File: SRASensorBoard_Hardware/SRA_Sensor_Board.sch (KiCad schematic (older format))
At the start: 70 parts, among them J1 USB_B_Micro, Q1 CSD17305Q5A, U1 LM3478MMX_NOPB, U2 OKI, U3 OKI, U4 TM4C129E_Launchpad, U5 MAX232, U6 IRF7821PbF

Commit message: Cleaned Some Things
Signatures and shem visual changes
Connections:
- wire segments 186 -> 185
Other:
- moved on the sheet: C1, C10, C11, C2, C3, C8, C9, D1, D10, D11, D12, D13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

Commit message: Updates
Updated traces on board

Changed resistor values to be in compliance with best practices

Regenerated STEP and GERBER files for updated board

Added TIVA and Connections text files
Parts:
- R10, R11, R12, R13, R14, R15, R16, R17, R18, R19, R20, R23, R24, R7: value 500 -> 510
- R9: value 500 -> 330
- U4: symbol MRDT_Shields:TM4C129E_Launchpad -> SRA_Sensor_Board-rescue:TM4C129E_Launchpad-MRDT_Shields
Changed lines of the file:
@@
 P 14850 5200
 F 0 "R20" H 14920 5246 50  0000 L CNN
-F 1 "500" H 14920 5155 50  0000 L CNN
+F 1 "510" H 14920 5155 50  0000 L CNN
 F 2 "Resistor_SMD:R_0603_1608Metric_Pad1.05x0.95mm_HandSolder" V 14780 5200 50  0001 C CNN
 F 3 "~" H 14850 5200 50  0001 C CNN
@@
 P 14500 5200
 F 0 "R19" H 14570 5246 50  0000 L CNN
-F 1 "500" H 14570 5155 50  0000 L CNN
+F 1 "510" H 14570 5155 50  0000 L CNN
 F 2 "Resistor_SMD:R_0603_1608Metric_Pad1.05x0.95mm_HandSolder" V 14430 5200 50  0001 C CNN
 F 3 "~" H 14500 5200 50  0001 C CNN
@@
 P 14150 5200
 F 0 "R18" H 14220 5246 50  0000 L CNN
-F 1 "500" H 14220 5155 50  0000 L CNN
+F 1 "510" H 14220 5155 50  0000 L CNN
 F 2 "Resistor_SMD:R_0603_1608Metric_Pad1.05x0.95mm_HandSolder" V 14080 5200 50  0001 C CNN
 F 3 "~" H 14150 5200 50  0001 C CNN
@@
 P 13800 5200
 F 0 "R17" H 13870 5246 50  0000 L CNN
-F 1 "500" H 13870 5155 50  0000 L CNN
+F 1 "510" H 13870 5155 50  0000 L CNN
 F 2 "Resistor_SMD:R_0603_1608Metric_Pad1.05x0.95mm_HandSolder" V 13730 5200 50  0001 C CNN
 F 3 "~" H 13800 5200 50  0001 C CNN
@@
 P 13450 5200
 F 0 "R16" H 13520 5246 50  0000 L CNN
-F 1 "500" H 13520 5155 50  0000 L CNN
+F 1 "510" H 13520 5155 50  0000 L CNN
 F 2 "Resistor_SMD:R_0603_1608Metric_Pad1.05x0.95mm_HandSolder" V 13380 5200 50  0001 C CNN
 F 3 "~" H 13450 5200 50  0001 C CNN
@@
 P 13100 5200
 F 0 "R15" H 13170 5246 50  0000 L CNN
-F 1 "500" H 13170 5155 50  0000 L CNN
+F 1 "510" H 13170 5155 50  0000 L CNN
 F 2 "Resistor_SMD:R_0603_1608Metric_Pad1.05x0.95mm_HandSolder" V 13030 5200 50  0001 C CNN
 F 3 "~" H 13100 5200 50  0001 C CNN
@@
 P 11100 5200
 F 0 "R13" H 11170 5246 50  0000 L CNN
-F 1 "500" H 11170 5155 50  0000 L CNN
+F 1 "510" H 11170 5155 50  0000 L CNN
 F 2 "Resistor_SMD:R_0603_1608Metric_Pad1.05x0.95mm_HandSolder" V 11030 5200 50  0001 C CNN
 F 3 "~" H 11100 5200 50  0001 C CNN
@@
 P 10750 5200
 F 0 "R12" H 10820 5246 50  0000 L CNN
-F 1 "500" H 10820 5155 50  0000 L CNN
+F 1 "510" H 10820 5155 50  0000 L CNN
 F 2 "Resistor_SMD:R_0603_1608Metric_Pad1.05x0.95mm_HandSolder" V 10680 5200 50  0001 C CNN
 F 3 "~" H 10750 5200 50  0001 C CNN
@@
 P 10400 5200
 F 0 "R11" H 10470 5246 50  0000 L CNN
-F 1 "500" H 10470 5155 50  0000 L CNN
+F 1 "510" H 10470 5155 50  0000 L CNN
 F 2 "Resistor_SMD:R_0603_1608Metric_Pad1.05x0.95mm_HandSolder" V 10330 5200 50  0001 C CNN
 F 3 "~" H 10400 5200 50  0001 C CNN
@@
 P 12700 5200
 F 0 "R14" H 12770 5246 50  0000 L CNN
-F 1 "500" H 12770 5155 50  0000 L CNN
+F 1 "510" H 12770 5155 50  0000 L CNN
 F 2 "Resistor_SMD:R_0603_1608Metric_Pad1.05x0.95mm_HandSolder" V 12630 5200 50  0001 C CNN
 F 3 "~" H 12700 5200 50  0001 C CNN
@@
 P 10050 5200
 F 0 "R10" H 10120 5246 50  0000 L CNN
-F 1 "500" H 10120 5155 50  0000 L CNN
+F 1 "510" H 10120 5155 50  0000 L CNN
 F 2 "Resistor_SMD:R_0603_1608Metric_Pad1.05x0.95mm_HandSolder" V 9980 5200 50  0001 C CNN
 F 3 "~" H 10050 5200 50  0001 C CNN
@@
 P 9700 5200
 F 0 "R9" H 9770 5246 50  0000 L CNN
-F 1 "500" H 9770 5155 50  0000 L CNN
+F 1 "330" H 9770 5155 50  0000 L CNN
 F 2 "Resistor_SMD:R_0603_1608Metric_Pad1.05x0.95mm_HandSolder" V 9630 5200 50  0001 C CNN
 F 3 "~" H 9700 5200 50  0001 C CNN
@@
 P 12300 5200
 F 0 "R24" H 12370 5246 50  0000 L CNN
-F 1 "500" H 12370 5155 50  0000 L CNN
+F 1 "510" H 12370 5155 50  0000 L CNN
 F 2 "Resistor_SMD:R_0603_1608Metric_Pad1.05x0.95mm_HandSolder" V 12230 5200 50  0001 C CNN
 F 3 "~" H 12300 5200 50  0001 C CNN
@@
 P 11900 5200
 F 0 "R23" H 11970 5246 50  0000 L CNN
-F 1 "500" H 11970 5155 50  0000 L CNN
+F 1 "510" H 11970 5155 50  0000 L CNN
 F 2 "Resistor_SMD:R_0603_1608Metric_Pad1.05x0.95mm_HandSolder" V 11830 5200 50  0001 C CNN
 F 3 "~" H 11900 5200 50  0001 C CNN
@@
 P 11500 5200
 F 0 "R7" H 11570 5246 50  0000 L CNN
-F 1 "500" H 11570 5155 50  0000 L CNN
+F 1 "510" H 11570 5155 50  0000 L CNN
 F 2 "Resistor_SMD:R_0603_1608Metric_Pad1.05x0.95mm_HandSolder" V 11430 5200 50  0001 C CNN
 F 3 "~" H 11500 5200 50  0001 C CNN
@@
 	9150 2650 9250 2650
 $Comp
-L MRDT_Shields:TM4C129E_Launchpad U4
+L SRA_Sensor_Board-rescue:TM4C129E_Launchpad-MRDT_Shields U4
 U 5 1 5DD6BB3C
 P 9450 3600
@@
 $EndComp
 $Comp
-L MRDT_Shields:TM4C129E_Launchpad U4
+L SRA_Sensor_Board-rescue:TM4C129E_Launchpad-MRDT_Shields U4
 U 6 1 5DD2931F
 P 9950 3600

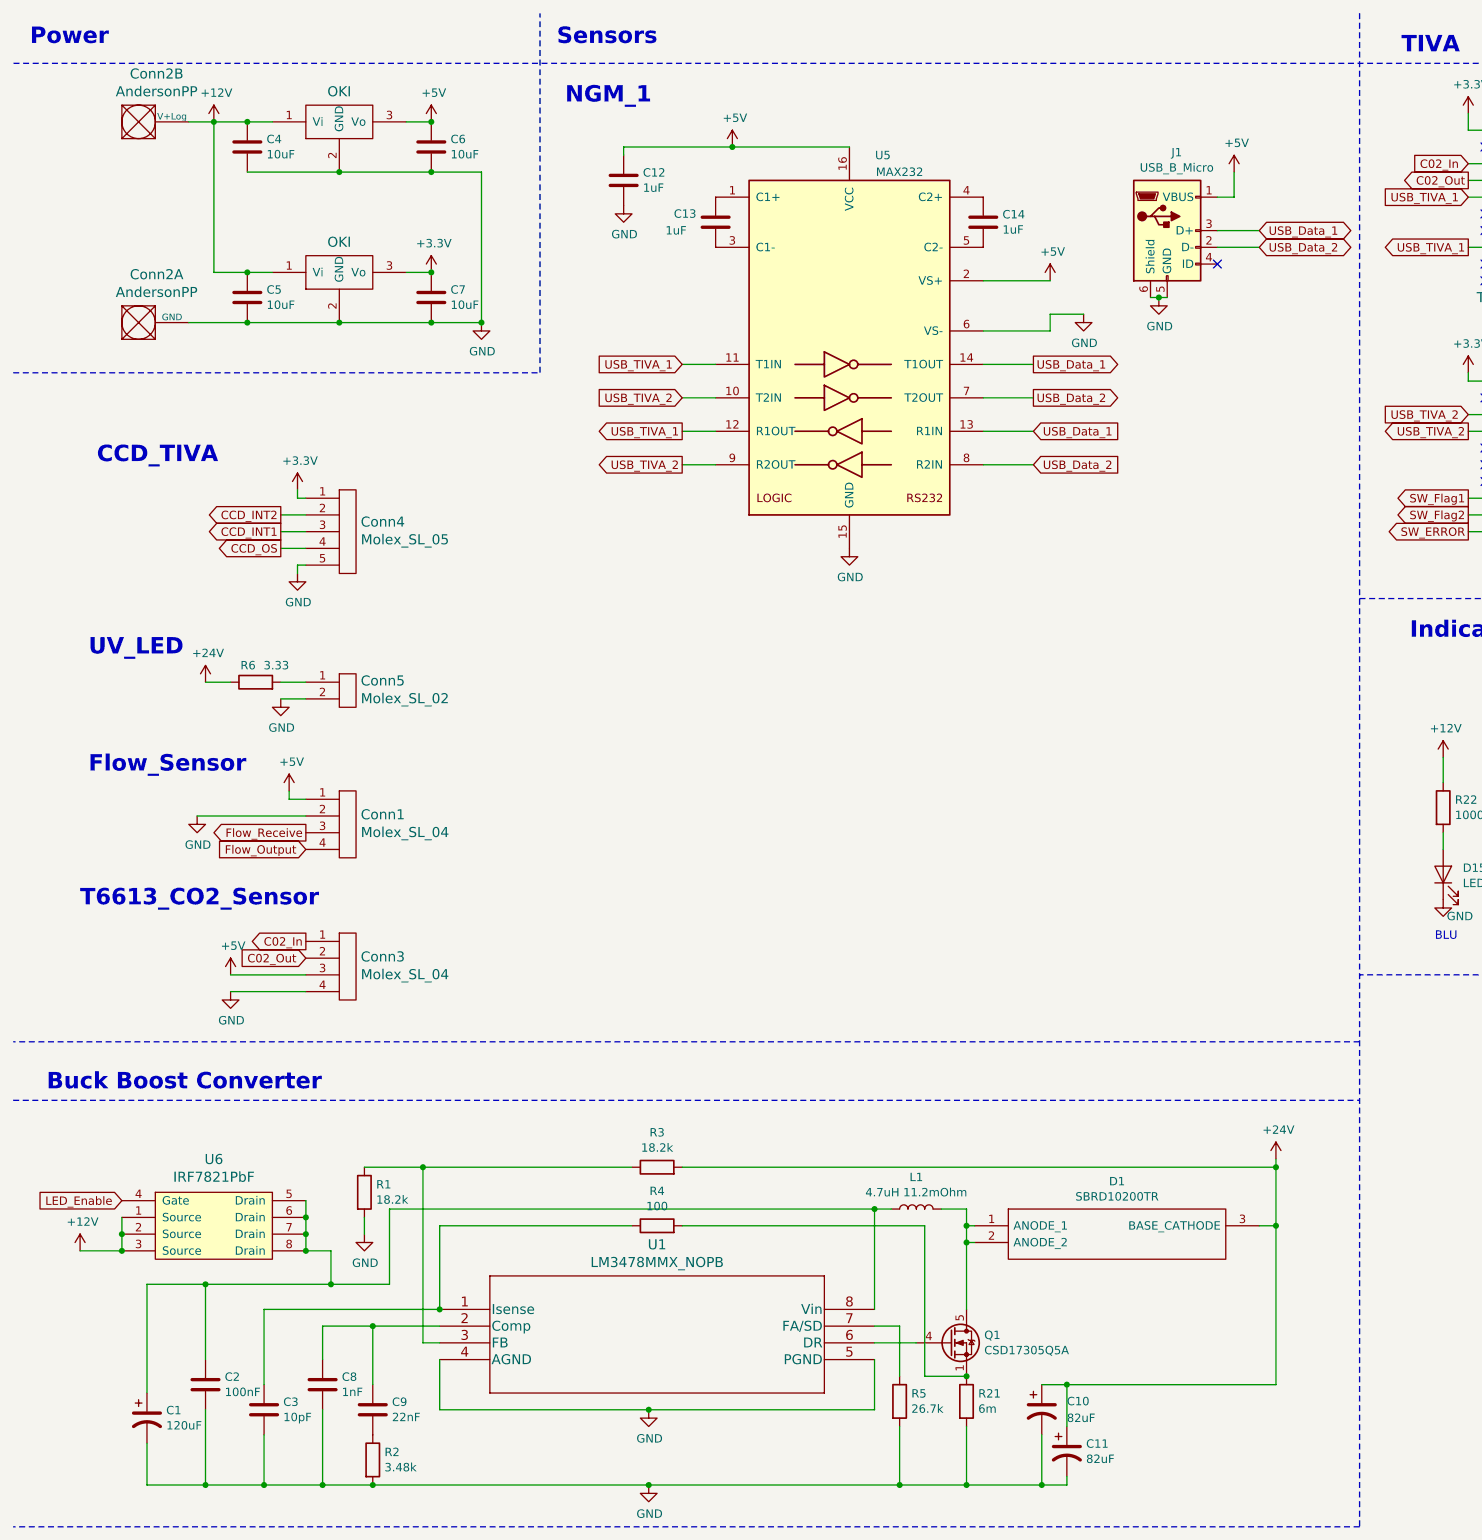
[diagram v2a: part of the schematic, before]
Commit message: Some Rev 2 schematic changes. Tivas and indicator leds still need updating
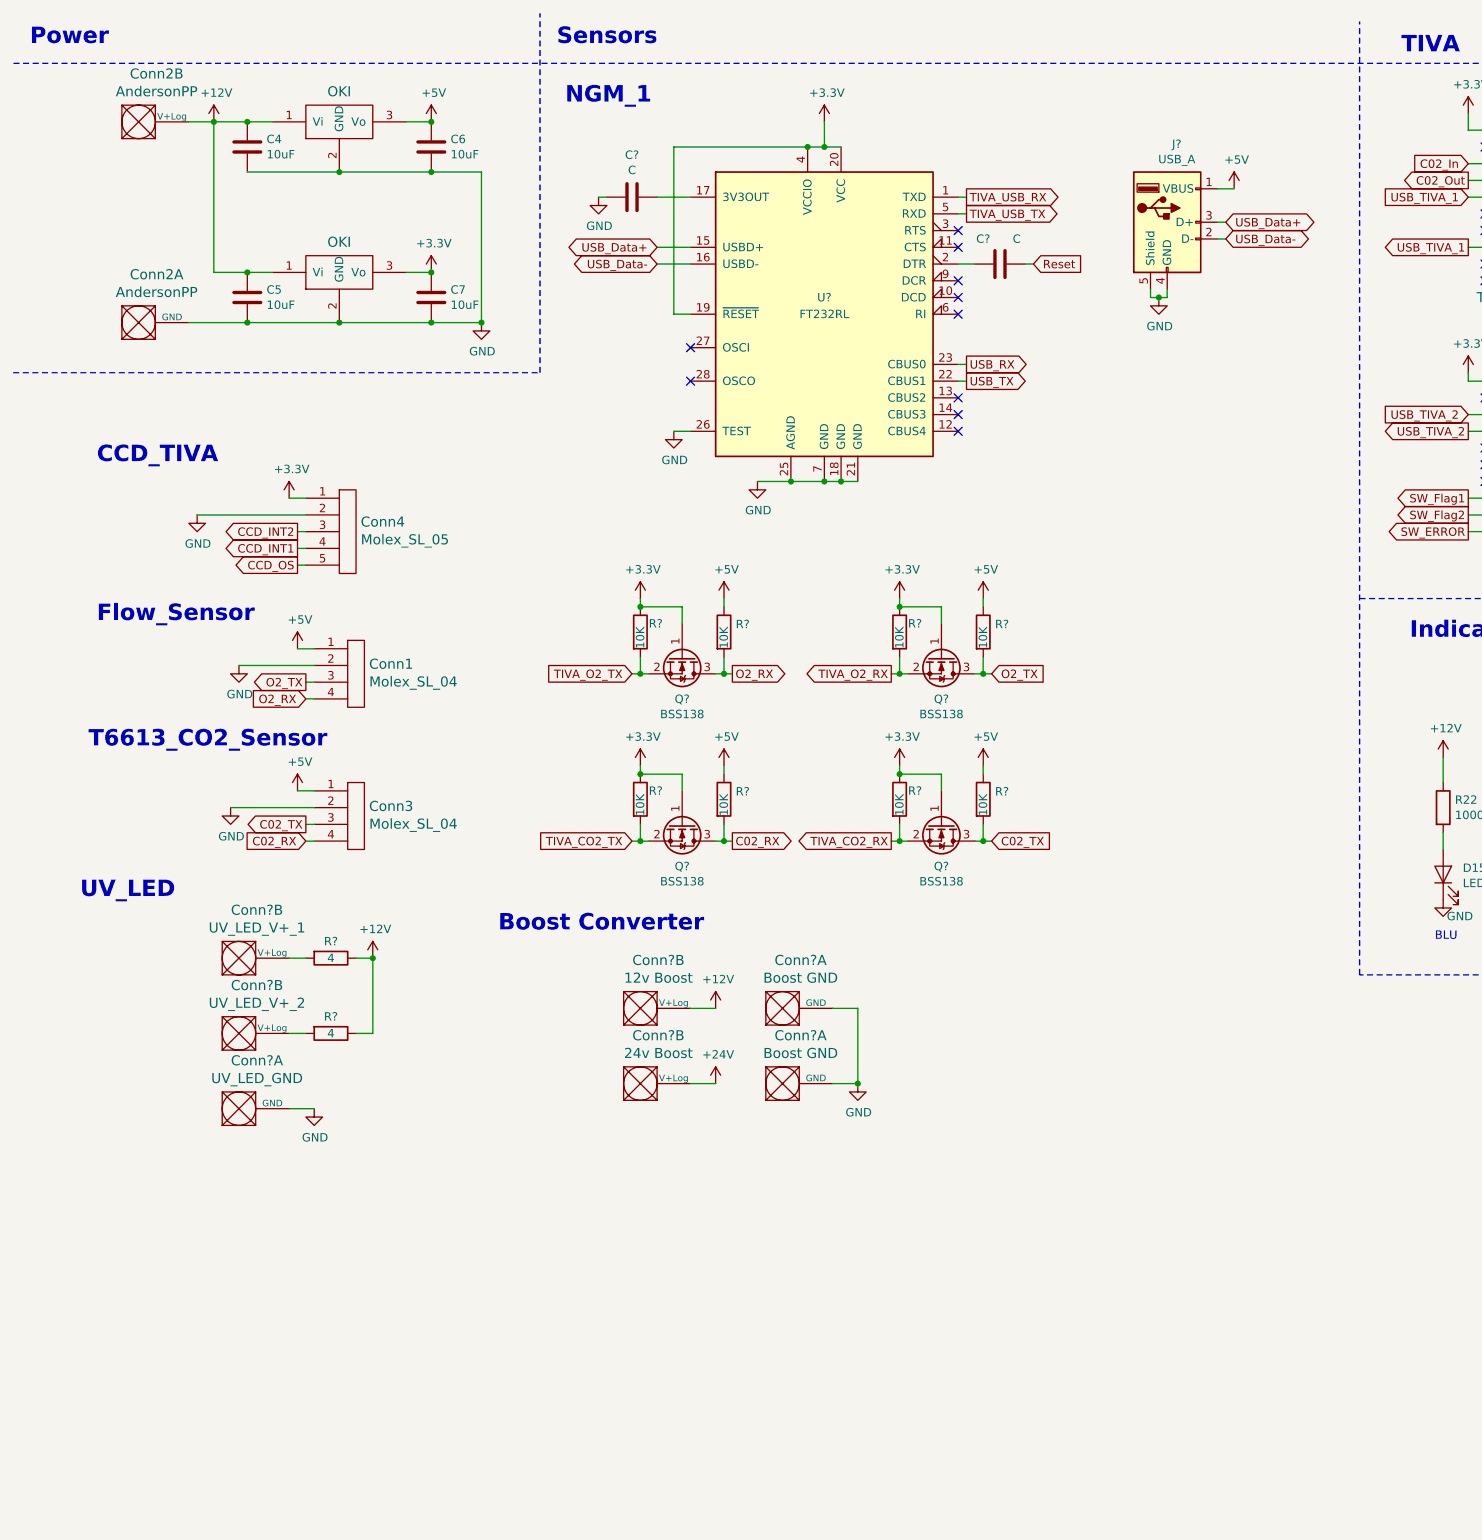
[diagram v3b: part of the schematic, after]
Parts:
- removed C1: 120uF, Capacitor_SMD:C_0603_1608Metric_Pad1.05x0.95mm_HandSolder, symbol Device:CP1
- removed C10, C11: 82uF, Capacitor_SMD:C_0603_1608Metric_Pad1.05x0.95mm_HandSolder, symbol Device:CP1
- removed C12, C13, C14: 1uF, Capacitor_SMD:C_0603_1608Metric_Pad1.05x0.95mm_HandSolder, symbol Device:C
- removed C2: 100nF, Capacitor_SMD:C_0603_1608Metric_Pad1.05x0.95mm_HandSolder, symbol Device:C
- removed C3: 10pF, Capacitor_SMD:C_0603_1608Metric_Pad1.05x0.95mm_HandSolder, symbol Device:C
- removed C8: 1nF, Capacitor_SMD:C_0603_1608Metric_Pad1.05x0.95mm_HandSolder, symbol Device:C
- removed C9: 22nF, Capacitor_SMD:C_0603_1608Metric_Pad1.05x0.95mm_HandSolder, symbol Device:C
- removed Conn5: Molex_SL_02, MRDT_Connectors:MOLEX_SL_02_Vertical, symbol MRDT_Connectors:Molex_SL_02
- removed D1: SBRD10200TR, MRDT_ICs:SMC_DPAK, symbol SBRD10200TR:SBRD10200TR
- removed J1: USB_B_Micro, Connector_USB:USB_Micro-B_Molex-105017-0001, symbol Connector:USB_B_Micro
- removed L1: 4.7uH 11.2mOhm, custom:Donald_Shaw_SRP1270, symbol Device:L
- removed Q1: CSD17305Q5A, Package_TO_SOT_SMD:TDSON-8-1, symbol Transistor_FET:CSD17305Q5A
- removed R1, R3: 18.2k, Resistor_SMD:R_0603_1608Metric_Pad1.05x0.95mm_HandSolder, symbol Device:R
- removed R2: 3.48k, Resistor_SMD:R_0603_1608Metric_Pad1.05x0.95mm_HandSolder, symbol Device:R
- removed R21: 6m, Resistor_SMD:R_0603_1608Metric_Pad1.05x0.95mm_HandSolder, symbol Device:R
- removed R4: 100, Resistor_SMD:R_0603_1608Metric_Pad1.05x0.95mm_HandSolder, symbol Device:R
- removed R5: 26.7k, Resistor_SMD:R_0603_1608Metric_Pad1.05x0.95mm_HandSolder, symbol Device:R
- removed R6: 3.33, Resistor_SMD:R_0603_1608Metric_Pad1.05x0.95mm_HandSolder, symbol Device:R
- removed U1: LM3478MMX_NOPB, custom:LM3478MMX&slash_NOPB, symbol SRA_Sensor_Board-rescue:LM3478MMX_NOPB-2019-10-10_22-50-45
- removed U5: MAX232, footprints:MAX232DR, symbol Interface_UART:MAX232
- removed U6: IRF7821PbF, footprints:IRF7821PBF, symbol MRDT_ICs:IRF7821PbF
- added C? (x2): C, symbol Device:C
- added Conn?: UV_LED_GND, symbol MRDT_Connectors:AndersonPP
- added Conn?: UV_LED_V+_1, symbol MRDT_Connectors:AndersonPP
- added Conn?: UV_LED_V+_2, symbol MRDT_Connectors:AndersonPP
- added Conn?: 12v Boost, symbol MRDT_Connectors:AndersonPP
- added Conn?: 24v Boost, symbol MRDT_Connectors:AndersonPP
- added Conn? (x2): Boost GND, symbol MRDT_Connectors:AndersonPP
- added J?: USB_A, symbol Connector:USB_A
- added Q? (x4): BSS138, Package_TO_SOT_SMD:SOT-23, symbol Transistor_FET:BSS138
- added R? (x8): 10K, symbol Device:R
- added R? (x2): 4, symbol Device:R
- added U?: FT232RL, Package_SO:SSOP-28_5.3x10.2mm_P0.65mm, symbol Interface_USB:FT232RL
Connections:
- net +12V: now also Conn?.2 (V+Log), R?.1, R?.1
- net +24V: now also Conn?.2 (V+Log)
- net +3V3: now also Q?.1 (G), Q?.1 (G), Q?.1 (G), Q?.1 (G), R?.1, R?.1, R?.1, R?.1, U?.19 (~RESET~), U?.20 (VCC), U?.4 (VCCIO)
- net +5V: now also Conn3.1, J?.1 (VBUS), R?.1, R?.1, R?.1, R?.1; no longer Conn3.3
- net C02_In: no longer Conn3.1
- net C02_Out: no longer Conn3.2
- net CCD_INT1: now also Conn4.4; no longer Conn4.3
- net CCD_INT2: now also Conn4.3; no longer Conn4.2
- net CCD_OS: now also Conn4.5; no longer Conn4.4
- net Flow_Output: no longer Conn1.4
- net Flow_Receive: no longer Conn1.3
- net GND: now also Conn3.2, Conn4.2, C?.2, Conn?.1 (GND), Conn?.1 (GND), Conn?.1 (GND), J?.4 (GND), J?.5 (Shield), U?.18 (GND), U?.21 (GND), U?.25 (AGND), U?.26 (TEST), U?.7 (GND); no longer Conn3.4, Conn4.5
- new net: C?.1, U?.17 (3V3OUT)
- new net: C?.2, U?.2 (DTR)
- new net: Conn?.2 (V+Log), R?.2 (x2)
- new net C02_RX: Conn3.4, Q?.3 (D), R?.2
- new net C02_TX: Conn3.3, Q?.3 (D), R?.2
- new net O2_RX: Conn1.4, Q?.3 (D), R?.2
- new net O2_TX: Conn1.3, Q?.3 (D), R?.2
- new net Reset: C?.1
- new net TIVA_CO2_RX: Q?.2 (S), R?.2
- new net TIVA_CO2_TX: Q?.2 (S), R?.2
- new net TIVA_O2_RX: Q?.2 (S), R?.2
- new net TIVA_O2_TX: Q?.2 (S), R?.2
- new net TIVA_USB_RX: U?.1 (TXD)
- new net TIVA_USB_TX: U?.5 (RXD)
- new net USB_Data+: J?.3 (D+), U?.15 (USBD+)
- new net USB_Data-: J?.2 (D-), U?.16 (USBD-)
- new net USB_RX: U?.23 (CBUS0)
- new net USB_TX: U?.22 (CBUS1)
- no-connect marks 58 -> 67
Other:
- note added: "Boost Converter"
- note removed: "Buck Boost Converter"
- moved on the sheet: Conn1, Conn3

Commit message: Schem Changes
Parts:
- added U1: LT1910, symbol MRDT_ICs:LT1910
- added U5: IRF7821PbF, symbol MRDT_ICs:IRF7821PbF
- C1: renamed from C?; value C -> 0.1 uF; footprint (none) -> Capacitor_SMD:C_0603_1608Metric_Pad1.05x0.95mm_HandSolder
- C2: renamed from C?; value C -> .1 uF; footprint (none) -> Capacitor_SMD:C_0603_1608Metric_Pad1.05x0.95mm_HandSolder
- Conn10, Conn11, Conn7, Conn8, Conn9: renamed from Conn?; footprint (none) -> MRDT_Connectors:Anderson_2_Horizontal_Stacked
- Conn5, Conn6: renamed from Conn?; footprint (none) -> MRDT_Connectors:Anderson_2_Horizontal_Side_by_Side
- J1: renamed from J?; footprint (none) -> Connector_USB:USB3_A_Molex_48393-001
- R1, R2, R21, R25, R26, R27, R3, R4, R5, R6: renamed from R?; footprint (none) -> Resistor_SMD:R_0603_1608Metric_Pad1.05x0.95mm_HandSolder
- gave numbers to parts that had none: 5
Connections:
- net +12V: now also U1.6 (SENSE), U1.8 (V+), U5.5 (Drain), U5.6 (Drain), U5.7 (Drain), U5.8 (Drain); no longer R3.1, R4.1
- net C02_In: no longer R14.1
- net C02_Out: no longer R24.1
- net C02_RX: now also R14.1
- net C02_TX: now also R24.1
- net Flow_Output: no longer R23.1
- net Flow_Receive: no longer R7.1
- net GND: now also U1.1 (GND)
- net LED_Enable: now also U1.4 (IN)
- net O2_RX: now also R7.1
- net O2_TX: now also R23.1
- net TIVA_USB_RX: now also R15.1, U4.PC6 (A1_5)
- net TIVA_USB_TX: now also R16.1, U4.PC7 (A1_8)
- removed net USB_TIVA_1: R16.1, U4.PC6 (A1_5), U4.PC7 (A1_8)
- removed net USB_TIVA_2: R15.1, U4.PP0 (A2_3), U4.PP1 (A2_4)
- new net: R3.1, R4.1, U5.1 (Source), U5.2 (Source), U5.3 (Source)
- new net: U1.5 (GATE), U5.4 (Gate)
- no-connect marks 67 -> 71
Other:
- note added: "GREEN"
- moved on the sheet: Conn10B, Conn11A, Conn5B, Conn6B, Conn7A, Conn8A, Conn9B, D15, D2, D3, D4, R10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

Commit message: Small changes to schmatic
Added names to sensors as well as part number if I found one. Schematic has been approved.
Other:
- note added: "CO2_Sensor\n"
- note added: "Flow Sensor"
- note added: "Methane Sensor"
- note added: "Telaire T6613"
- note removed: "Flow_Sensor"
- note removed: "T6613_CO2_Sensor\n"
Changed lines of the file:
@@
 Wire Notes Line
 	16100 750  450  750
-Text Notes 3750 1000 0    98   ~ 20
+Text Notes 5700 1000 0    98   ~ 20
 NGM_1
 Wire Notes Line
@@
 	1    0    0    -1
 $EndComp
-Text Notes 950  4100 0    98   ~ 20
-Flow_Sensor
+Text Notes 650  4300 0    98   ~ 20
+Flow Sensor
 $Comp
 L MRDT_Connectors:Molex_SL_04 Conn3
@@
 	1    0    0    -1
 $EndComp
-Text Notes 900  4850 0    98   ~ 20
-T6613_CO2_Sensor\n
+Text Notes 550  5350 0    98   ~ 20
+Telaire T6613
 Text GLabel 2200 5300 0    50   Output ~ 0
 C02_TX
@@
 NoConn ~ 9250 2950
 NoConn ~ 9250 2850
+Text Notes 600  5150 0    98   ~ 20
+CO2_Sensor\n
+Text Notes 3750 950  0    98   ~ 20
+Methane Sensor
 $EndSCHEMATC
